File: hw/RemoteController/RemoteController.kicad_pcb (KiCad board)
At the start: 2 copper layers, 100 x 75 mm, 145 parts, among them J1 Conn_01x04_Pin, J2 Conn_01x04_Pin, J4 BWSMA-KWE-Z3.5*4.2, SW3 TC-6610-6*6*8-300g, SW4 TC-6610-6*6*8-300g, SW5 TC-6610-6*6*8-300g, SW6 TC-6610-6*6*8-300g, U1 LM358, U11 LM358, U12 MAX1473EUI+, U13 nRF52810-QFxx, U14 LM358, U15 LM358, U17 AD8313xRM, U18 LM358, U2 TPS562200, U3 SPF5043Z, U5 XA17-G4K, U6 MAX7044AKA, U8 AD8313xRM, U9 GVA-63, Y1 32 MHz, Y2 6.6128 MHz, Y3 10.7 MHz, Y4 13.56 MHz, Y5 32.768 KHz

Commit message: remote_ctrl: basic PCB shape
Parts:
- added H1: MountingHole, MountingHole:MountingHole_2.2mm_M2, F.Cu at (116.2, 112.7)
- added H2: MountingHole, MountingHole:MountingHole_2.2mm_M2, F.Cu at (116.2, 118.7)
- added H3: MountingHole, MountingHole:MountingHole_2.2mm_M2, F.Cu at (116.2, 124.6)
- added H4: MountingHole, MountingHole:MountingHole_2.2mm_M2, F.Cu at (116.2, 130.6)
- C27, U12, U5, U6, Y2, Y3, Y4: moved to B.Cu
- moved C27 208.1 mm to (221.2, 41.8), turned to 90 degrees
- moved U6 188.6 mm to (211.0, 43.5)
- moved Y4 170.7 mm to (210.9, 47.6), turned to 180 degrees
- moved Y3 169.6 mm to (202.8, 38.8), turned to 180 degrees
- moved U5 167.9 mm to (221.2, 45.2), turned to 90 degrees
- moved Y2 157.7 mm to (202.5, 54.8), turned to 180 degrees
- moved Y1 143.7 mm to (169.5, 37.5), turned to 180 degrees
- moved U8 139.6 mm to (165.9, 45.8)
- moved U12 138.6 mm to (202.6, 46.5)
- moved U1 126.1 mm to (152.2, 39.0)
- moved U11 120.3 mm to (144.5, 39.0)
- moved SW6 108.5 mm to (189.8, 62.8)
- moved SW3 105.1 mm to (179.2, 67.0)
- moved SW4 99.9 mm to (179.2, 57.8)
- moved U14 90.2 mm to (115.3, 53.0)
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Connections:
- J2 pad 2: +3V3 -> +3V0

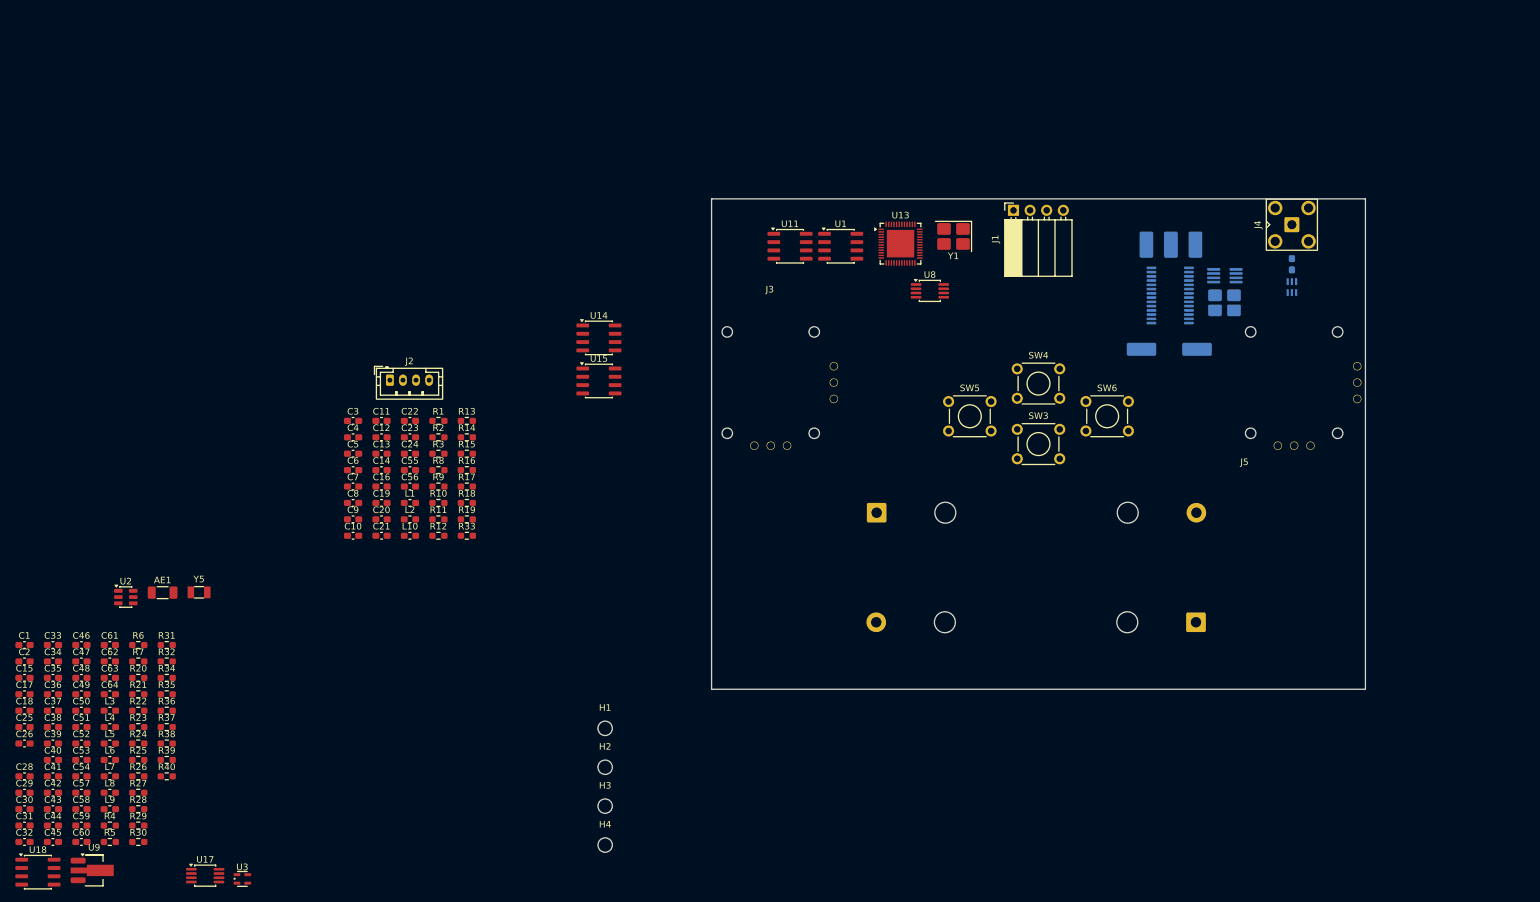
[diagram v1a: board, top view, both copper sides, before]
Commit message: remote_ctrl: start laying out RF components
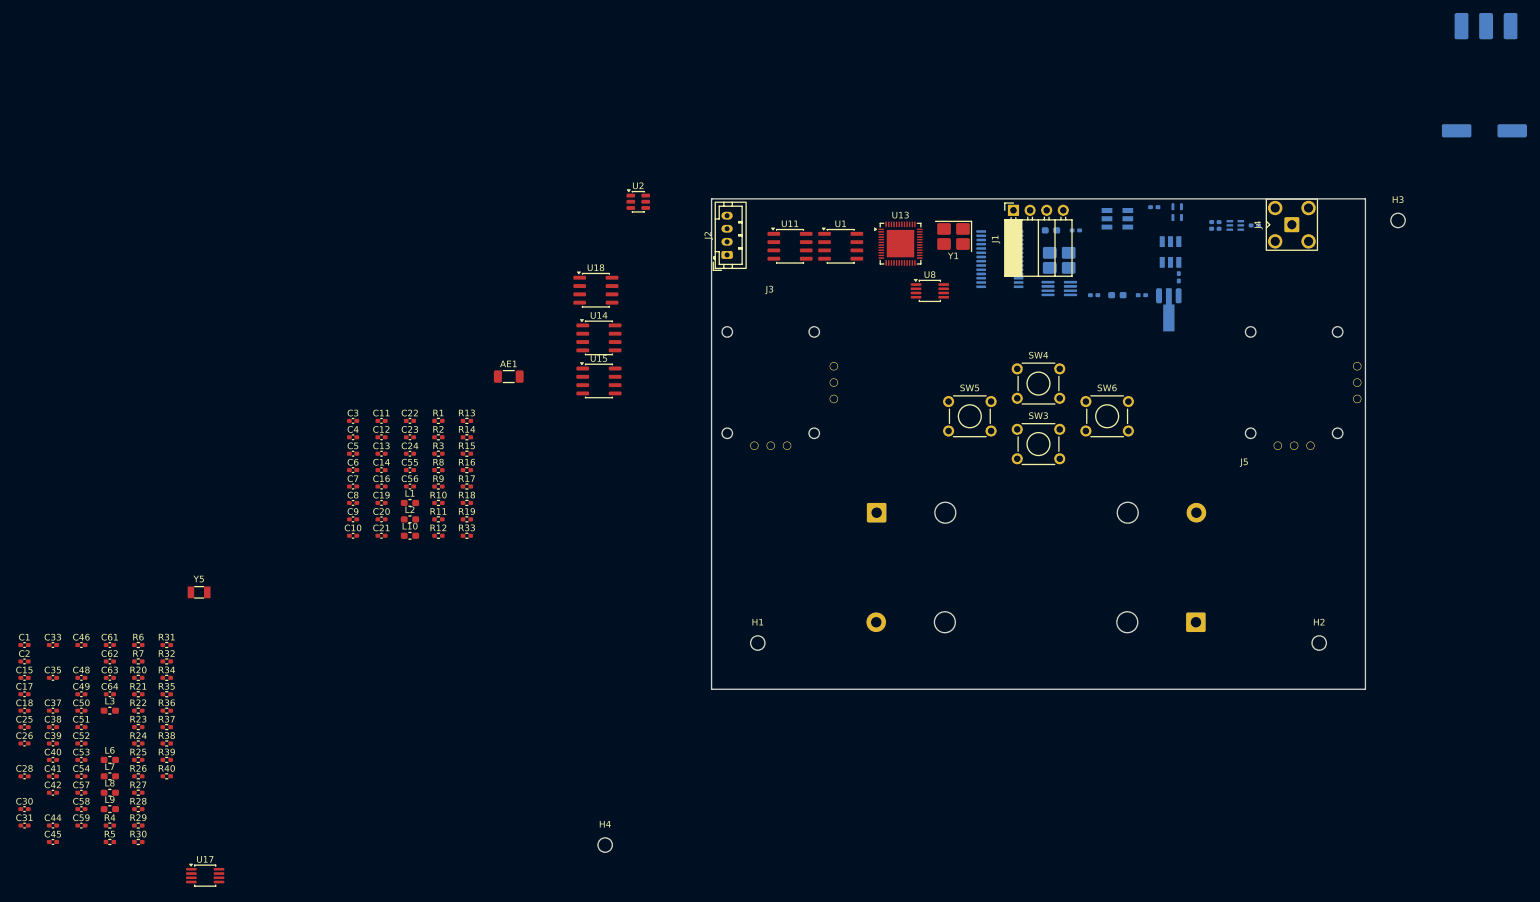
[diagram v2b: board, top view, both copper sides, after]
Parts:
- added U10: H3-TCD-12-222X+, RF_Mini-Circuits:Mini-Circuits_DB1627, B.Cu at (202.7, 39.9)
- added U16: H3-TCD-12-222X+, RF_Mini-Circuits:Mini-Circuits_DB1627, B.Cu at (194.6, 34.8)
- C1, C10, C11, C12, C13, C14, C15, C16, C17, C18, C19, C2, C20, C21, C22, C23, C24, C25, C26, C27, C28, C3, C30, C31, C33, C35, C37, C38, C39, C4, C40, C41, C42, C44, C45, C46, C48, C49, C5, C50, C51, C52, C53, C54, C55, C56, C57, C58, C59, C6, C61, C62, C63, C64, C7, C8, C9: footprint Capacitor_SMD:C_0603_1608Metric_Pad1.08x0.95mm_HandSolder -> Capacitor_SMD:C_0402_1005Metric_Pad0.74x0.62mm_HandSolder
- C29, C32, C34, C36, C43, C47, C60: footprint Capacitor_SMD:C_0603_1608Metric_Pad1.08x0.95mm_HandSolder -> Capacitor_SMD:C_0402_1005Metric_Pad0.74x0.62mm_HandSolder; moved to B.Cu
- L4, L5, U3, U9: moved to B.Cu
- R1, R10, R11, R12, R13, R14, R15, R16, R17, R18, R19, R2, R20, R21, R22, R23, R24, R25, R26, R27, R28, R29, R3, R30, R31, R32, R33, R34, R35, R36, R37, R38, R39, R4, R40, R5, R6, R7, R8, R9: footprint Resistor_SMD:R_0603_1608Metric_Pad0.98x0.95mm_HandSolder -> Resistor_SMD:R_0402_1005Metric_Pad0.72x0.64mm_HandSolder
- moved C32 204.9 mm to (209.6, 36.3)
- moved C60 190.7 mm to (200.2, 33.0)
- moved C34 190.0 mm to (209.6, 35.3)
- moved U9 185.2 mm to (202.4, 49.0), turned to -90 degrees
- moved C43 184.2 mm to (198.3, 46.5)
- moved C29 182.3 mm to (188.2, 36.6)
- moved C47 177.8 mm to (204.0, 43.7), turned to -90 degrees
- moved U3 175.6 mm to (203.7, 33.8), turned to 90 degrees
- moved C36 170.5 mm to (191.0, 46.5), turned to 180 degrees
- moved L4 167.6 mm to (194.6, 46.5)
- moved L5 163.9 mm to (184.4, 36.6), turned to 180 degrees
- moved H3 150.8 mm to (237.5, 35.1)
- moved U18 123.3 mm to (114.8, 45.7)
- moved H2 110.8 mm to (225.4, 99.7)
- moved U2 99.0 mm to (121.3, 32.2)
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
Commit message: remote_ctrl: add RF net class
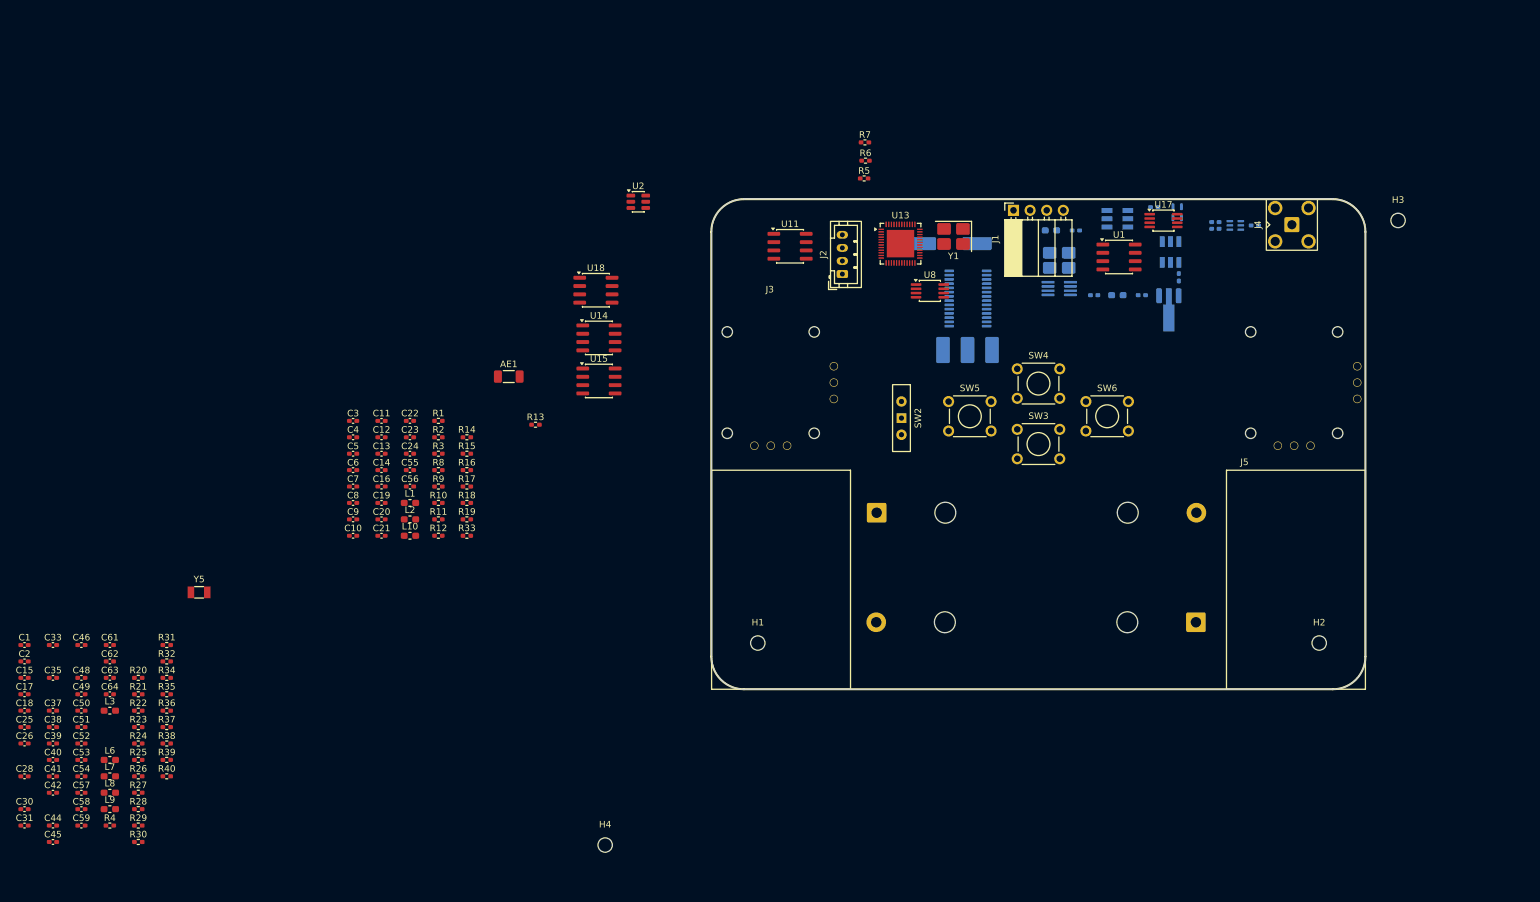
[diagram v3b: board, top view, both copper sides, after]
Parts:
- added SW2: ST-0-102-A01-T000-LF, Button_Switch_THT:SW_Slide-03_Wuerth-WS-SLTV_10x2.5x6.4_P2.54mm, F.Cu at (161.5, 65.3)
- moved U17 177.5 mm to (201.6, 35.1)
- moved R5 153.6 mm to (155.8, 28.6)
- moved R7 136.6 mm to (156.0, 23.1)
- moved R6 133.6 mm to (156.0, 25.9)
- moved Y3 93.5 mm to (171.6, 54.9), turned to 0 degrees
- moved Y2 83.7 mm to (168.8, 38.6), turned to 0 degrees
- moved U1 42.6 mm to (194.8, 40.6)
- moved J2 17.9 mm to (152.5, 43.2)
- moved R13 10.5 mm to (105.6, 66.3)
- moved U12 7.76 mm to (171.7, 47.0)
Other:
- outline, holes or cut-outs redrawn
- copper layers 2 -> 4

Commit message: remote_ctrl: half way to placement, replace max1473 wit, micrf220
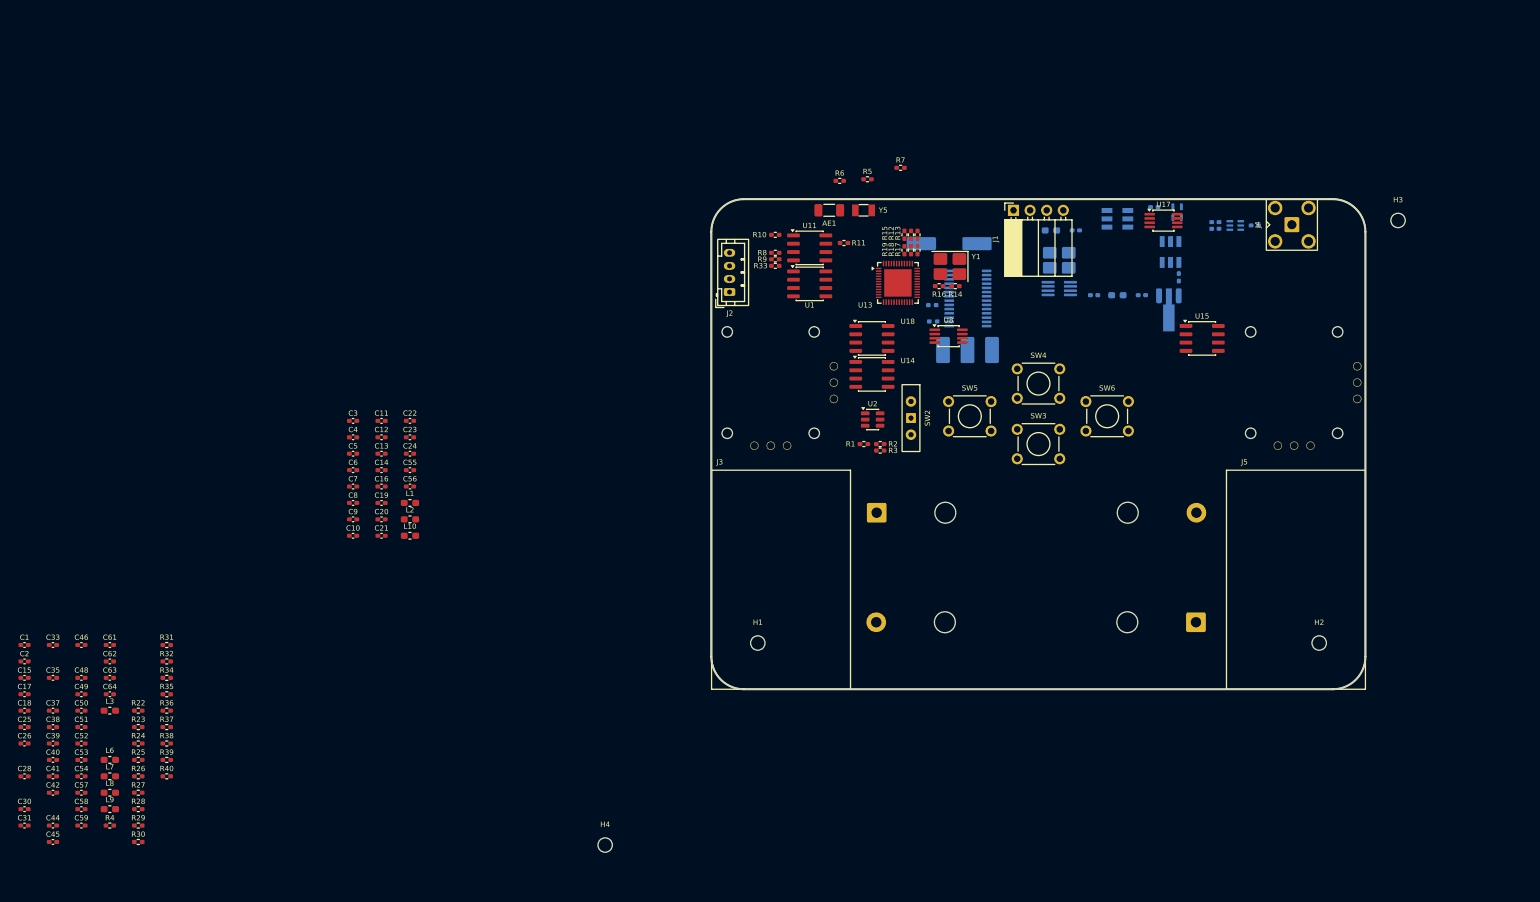
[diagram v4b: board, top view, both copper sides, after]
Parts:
- R20, R21: moved to B.Cu
- moved R21 134.3 mm to (166.4, 50.5), turned to 180 degrees
- moved R20 134.1 mm to (166.2, 48.0), turned to 180 degrees
- moved Y5 117.2 mm to (155.8, 33.5)
- moved U15 92.5 mm to (207.5, 53.1)
- moved R12 85.7 mm to (163.0, 37.2), turned to -90 degrees
- moved R19 78.6 mm to (162.0, 39.6), turned to 90 degrees
- moved R14 78.2 mm to (169.8, 45.1), turned to 180 degrees
- moved R18 78.2 mm to (163.0, 39.6), turned to 90 degrees
- moved R17 77.8 mm to (164.0, 39.6), turned to 90 degrees
- moved R16 77.5 mm to (167.3, 45.1)
- moved R11 75.1 mm to (152.8, 38.5)
- moved R15 74.8 mm to (162.0, 37.2), turned to -90 degrees
- moved R2 67.6 mm to (158.3, 69.2)
- moved R3 67.6 mm to (158.3, 70.2), turned to 180 degrees
- moved R10 65.9 mm to (142.2, 37.2)
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
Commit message: remote_ctrl: continue placemen
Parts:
- removed C28, C29, C49: 100P, Capacitor_SMD:C_0402_1005Metric_Pad0.74x0.62mm_HandSolder
- removed C40: 10N, Capacitor_SMD:C_0402_1005Metric_Pad0.74x0.62mm_HandSolder
- removed C41, C42: 220P, Capacitor_SMD:C_0402_1005Metric_Pad0.74x0.62mm_HandSolder
- removed C50: 2P7, Capacitor_SMD:C_0402_1005Metric_Pad0.74x0.62mm_HandSolder
- removed L6, L7: 15N, Inductor_SMD:L_0603_1608Metric_Pad1.05x0.95mm_HandSolder
- removed R20: 5K1, Resistor_SMD:R_0402_1005Metric_Pad0.72x0.64mm_HandSolder
- removed R21, R22, R23, R24: 0R, Resistor_SMD:R_0402_1005Metric_Pad0.72x0.64mm_HandSolder
- removed U12: MAX1473EUI+, Package_SO:TSSOP-28_4.4x9.7mm_P0.65mm
- removed Y3: 10.7 MHz, Crystal:Resonator_SMD_Murata_SFECV-3Pin_6.9x2.9mm_HandSoldering
- added R41: 100R, Resistor_SMD:R_0402_1005Metric_Pad0.72x0.64mm_HandSolder, B.Cu at (191.3, 41.5)
- added U4: MICRF220AYQS, Package_SO:QSOP-16_3.9x4.9mm_P0.635mm, B.Cu at (188.8, 38.0)
- C1, C2: value C -> 10P
- C17: value 1500P -> 10P; moved to B.Cu
- C25: value 470P -> 10P; moved to B.Cu
- C33: value 470N -> 100N; moved to B.Cu
- C35: value 10N -> 1000P; moved to B.Cu
- C38: value 10N -> 100N
- C39: value 100N -> 4U7; moved to B.Cu
- C44, C45, C46, C53, L3, L8, L9, R25, R26, R27, R34, R37, R4, R5, R6, R7, U17, U8: moved to B.Cu
- L5: value 56N -> VHF160808H39NJT
- Y2: value 6.6128 MHz -> L327S13CU11L; footprint Crystal:Crystal_SMD_HC49-SD -> Crystal:Crystal_SMD_3225-4Pin_3.2x2.5mm_HandSoldering
- moved R26 224.1 mm to (243.7, 16.8), turned to 180 degrees
- moved R25 219.6 mm to (242.2, 21.2)
- moved C45 200.1 mm to (214.2, 48.0), turned to 180 degrees
- moved C44 198.7 mm to (214.2, 49.0), turned to 180 degrees
- moved L8 186.9 mm to (212.8, 50.2), turned to 180 degrees
- moved C46 185.8 mm to (214.2, 47.0), turned to 180 degrees
- moved L9 185.5 mm to (204.5, 38.5)
- moved R4 184.7 mm to (205.2, 44.2), turned to 90 degrees
- moved C25 181.5 mm to (191.3, 34.7)
- moved C53 178.9 mm to (200.8, 47.5), turned to 180 degrees
- moved C38 177.9 mm to (193.7, 39.0), turned to -90 degrees
- moved C35 176.2 mm to (194.3, 37.0)
- moved C17 174.8 mm to (186.3, 34.7)
- moved R27 172.6 mm to (200.8, 48.5)
- moved C39 171.1 mm to (183.8, 36.7), turned to 90 degrees
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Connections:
- net /RXEN renamed /RF_SEL0
- net /~{TXEN} renamed /RF_SEL1
- C17 pad 1: Net-(U12-IFIN1) -> GND
- C17 pad 2: GND -> Net-(U4-RO2)
- C25 pad 1: Net-(U12-DFFB) -> GND
- C25 pad 2: Net-(U12-DFO) -> Net-(U4-RO1)
- C35 pad 1: GND -> Net-(U4-ANT)
- C35 pad 2: +3V0 -> Net-(U16-OUT)
- C38 pad 1: GND -> +3V0
- C38 pad 2: +3V0 -> GND
- C39 pad 1: GND -> Net-(U4-CAGC)
- C39 pad 2: +3V0 -> GND
- L5 pad 1: Net-(C29-Pad1) -> GND
- L5 pad 2: Net-(U12-LNAIN) -> Net-(U4-ANT)
- U13 pad 12: +3V0 -> /RX_BW_SEL1
- U13 pad 14: /PDOUT -> /RX_BW_SEL0
- U13 pad 15: /AGCDIS -> /RX_SQUELCH
- U13 pad 16: unconnected-(U13-P0.13-Pad16) -> /~{RX_SHDN}
- U13 pad 40: unconnected-(U13-P0.28/AIN4-Pad40) -> /RX_RSSI
- Y2 pad 1: Net-(U12-XTAL2-Pad28) -> Net-(U4-RO2)
- Y2 pad 2: Net-(U12-XTAL2-Pad1) -> GND
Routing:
- net Net-(U6-PAOUT): track 0.00 -> 8.60 mm
- net Net-(U5-RF1): track 0.00 -> 5.84 mm
- net Net-(U16-CPL): track 0.00 -> 5.78 mm
- net Net-(J4-In): track 0.00 -> 4.95 mm
- net Net-(U4-ANT): track 0.00 -> 4.94 mm
- net Net-(C47-Pad1): track 0.00 -> 3.16 mm
- net Net-(C53-Pad1): track 0.00 -> 2.84 mm
- net Net-(U16-OUT): track 0.00 -> 2.55 mm
- net Net-(U17-INLO): track 0.00 -> 2.40 mm
- net Net-(U16-IN): track 0.00 -> 2.15 mm
- net Net-(C31-Pad1): track 0.00 -> 2.04 mm
- net Net-(U8-INHI): track 0.00 -> 2.00 mm
- net Net-(C43-Pad2): track 0.00 -> 1.95 mm
- net Net-(C34-Pad1): track 0.00 -> 1.88 mm
- net Net-(U10-OUT): track 0.00 -> 1.85 mm
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- added copper zone on B.Cu, net GND

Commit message: remote_ctrl: pre-outline modifications
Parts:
- AE1, C1, C10, C11, C12, C13, C14, C15, C16, C18, C19, C2, C20, C22, C23, C24, C26, C3, C30, C31, C37, C4, C48, C5, C55, C6, C61, C62, C63, C64, C7, C8, C9, L1, L10, L2, R1, R10, R11, R12, R13, R14, R15, R16, R17, R18, R19, R2, R28, R29, R3, R31, R32, R33, R38, R39, R8, R9, U1, U11, U13, U14, U15, U18, U2, Y1, Y5: moved to B.Cu
- moved C30 144.2 mm to (165.2, 82.6), turned to -90 degrees
- moved C31 140.9 mm to (160.7, 81.9)
- moved C26 138.4 mm to (162.2, 83.6), turned to -90 degrees
- moved C18 136.4 mm to (161.2, 83.6), turned to -90 degrees
- moved C15 134.5 mm to (160.2, 83.6), turned to -90 degrees
- moved C64 131.1 mm to (163.8, 63.0), turned to -90 degrees
- moved C62 130.4 mm to (164.8, 63.0), turned to -90 degrees
- moved C48 130.2 mm to (163.6, 78.5), turned to 180 degrees
- moved C63 129.3 mm to (162.8, 63.0), turned to -90 degrees
- moved C2 128.6 mm to (153.5, 77.0), turned to 180 degrees
- moved C1 124.5 mm to (149.8, 77.0), turned to 180 degrees
- moved C37 120.4 mm to (148.0, 78.7), turned to 90 degrees
- moved R25 100.0 mm to (160.8, 79.2), turned to 180 degrees
- moved R26 98.5 mm to (163.8, 74.2)
- moved R28 75.6 mm to (105.3, 80.8), turned to 180 degrees
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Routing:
- net Net-(J4-In): track 4.95 -> 0.14 mm
- net +3V0: track 0.00 -> 4.43 mm, vias 0 -> 1
- net Net-(U6-PAOUT): track 8.60 -> 6.86 mm
- net Net-(C53-Pad1): track 2.84 -> 4.02 mm
- net Net-(U16-CPL): track 5.78 -> 6.65 mm
- net Net-(U17-INLO): track 2.40 -> 3.26 mm

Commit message: remote_ctrl: finish placement
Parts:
- removed SW3, SW4, SW5: TC-6610-6*6*8-300g, Button_Switch_THT:SW_TH_Tactile_Omron_B3F-106x
- added SW7: TS-1088-AR02016, Button_Switch_SMD:SW_SPST_TS-1088-xR020, F.Cu at (141.8, 112.5)
- added SW8: TS-1088-AR02016, Button_Switch_SMD:SW_SPST_TS-1088-xR020, F.Cu at (149.2, 112.5)
- added SW9: TS-1088-AR02016, Button_Switch_SMD:SW_SPST_TS-1088-xR020, F.Cu at (156.8, 112.5)
- C54, C59: moved to B.Cu
- SW6: value TC-6610-6*6*8-300g -> TS-1088-AR02016; footprint Button_Switch_THT:SW_TH_Tactile_Omron_B3F-106x -> Button_Switch_SMD:SW_SPST_TS-1088-xR020
- moved C59 138.2 mm to (163.2, 73.5), turned to 90 degrees
- moved C58 137.4 mm to (162.2, 70.5)
- moved C57 135.6 mm to (162.2, 72.8)
- moved C52 132.3 mm to (162.2, 75.0)
- moved C51 130.5 mm to (162.0, 78.0)
- moved C54 106.3 mm to (129.8, 69.8), turned to 90 degrees
- moved R28 35.1 mm to (139.2, 71.8), turned to 0 degrees
- moved SW6 29.9 mm to (134.2, 112.5)
- moved R38 25.3 mm to (130.5, 77.2), turned to 0 degrees
- moved R30 4.00 mm to (162.0, 79.0)
- moved R39 2.09 mm to (130.5, 76.2), turned to 180 degrees
- moved SW2 1.68 mm to (125.3, 97.5)
- moved R26 1.66 mm to (162.7, 75.5)
- moved C38 1.12 mm to (156.8, 67.5), turned to 0 degrees
- moved R25 1.00 mm to (159.8, 79.2)
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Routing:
- net Net-(C60-Pad2): track 1.58 -> 4.13 mm
- net Net-(C53-Pad1): track 4.02 -> 4.98 mm
- net Net-(U17-INLO): track 3.26 -> 4.01 mm
- net Net-(U16-CPL): track 6.65 -> 7.40 mm
- net GND: vias 16 -> 50
- added copper zone on In1.Cu, net +3V0
- added copper zone on In2.Cu, net GND
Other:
- board text added: "CNCL"
- board text added: "OK"
